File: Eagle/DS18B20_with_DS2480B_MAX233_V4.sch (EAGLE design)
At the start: 15 parts, among them IC1 MAX233AEWP, IC2 DS2480B, IC3 DS18B20, IC4 MAX9940

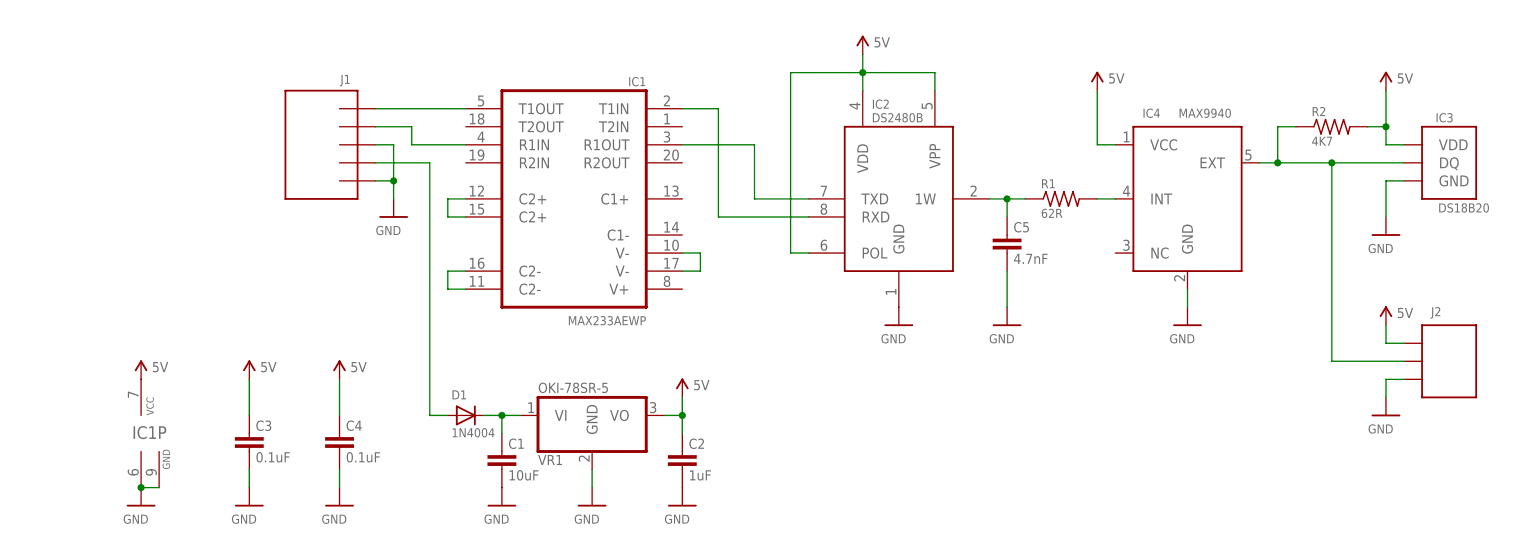
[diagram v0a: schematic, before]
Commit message: Design with MAX9940 protection
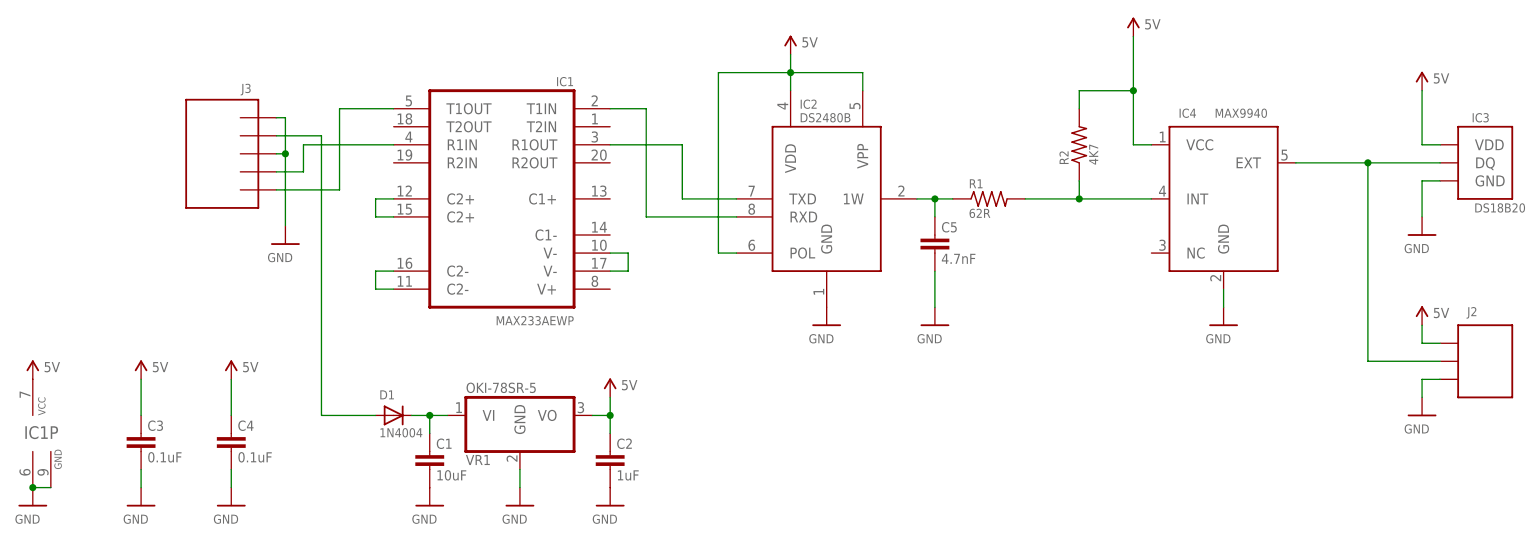
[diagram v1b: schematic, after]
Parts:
- removed J1: (no value), AU2016:DF1B-5P
- added J3: (no value), AU2016:DF1B-5P
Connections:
- net GND: now also J3.P$3, J3.P$5; no longer J1.P$1, J1.P$3
- net N$1: now also J3.P$4; no longer J1.P$2
- net N$13: now also R2.1
- net N$14: no longer R2.1
- net N$4: now also J3.P$1; no longer J1.P$5
- net N$5: now also J3.P$2; no longer J1.P$4
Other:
- moved on the sheet: C1, C2, C3, C4, C5, D1, IC1, IC1P, IC2, IC3, IC4, J2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
